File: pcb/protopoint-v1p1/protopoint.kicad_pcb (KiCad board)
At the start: 4 copper layers, 31.8 x 27.5 mm, 52 parts, among them T1 HHM1595A1, U1 STM32F031G4U6, U2 LXDC2HL, U3 DW1000, U4 SKY13317, U5 ProtoPoint_Module, X1 CRYSTAL_SMD_4, X2 CRYSTAL_SMD_4

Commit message: routing more signals out to castellations
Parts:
- C10, C17: value 12pF -> 100pF
- C11: value 12pF -> 10pF
- C16, C9: value 12pF -> 0.1uF
- C25, C26: value C_Small -> 12pF
- U1: value STM32F031G4U6 -> STM32F031G6U6
- X1: value CRYSTAL_SMD_4 -> 38.4M
- X2: value CRYSTAL_SMD_4 -> 16M
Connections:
- net V3P3 renamed VDD
- net VDDLDO1 renamed V1P8
- U5 pad 20: (no net) -> /SPI1_MOSI
- U5 pad 21: (no net) -> /SPI1_MISO
- U5 pad 22: (no net) -> /SPI1_CLK
- U5 pad 23: (no net) -> /~SPI1_SS
- U5 pad 24: (no net) -> /~DW_RST
- U5 pad 39: (no net) -> /DW_IRQ
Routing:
- net /SPI1_MOSI: track 11.0 -> 26.6 mm, vias 0 -> 1
- net /SPI1_MISO: track 11.4 -> 25.8 mm, vias 0 -> 1
- net /SPI1_CLK: track 11.8 -> 25.0 mm, vias 0 -> 1
- net /~SPI1_SS: track 8.28 -> 20.6 mm
- net /~DW_RST: track 5.01 -> 15.6 mm, vias 0 -> 1
- net V1P8: track 47.3 -> 41.5 mm
- net /DW_IRQ: track 13.1 -> 17.7 mm
- net VDD: track 137.5 -> 133.6 mm

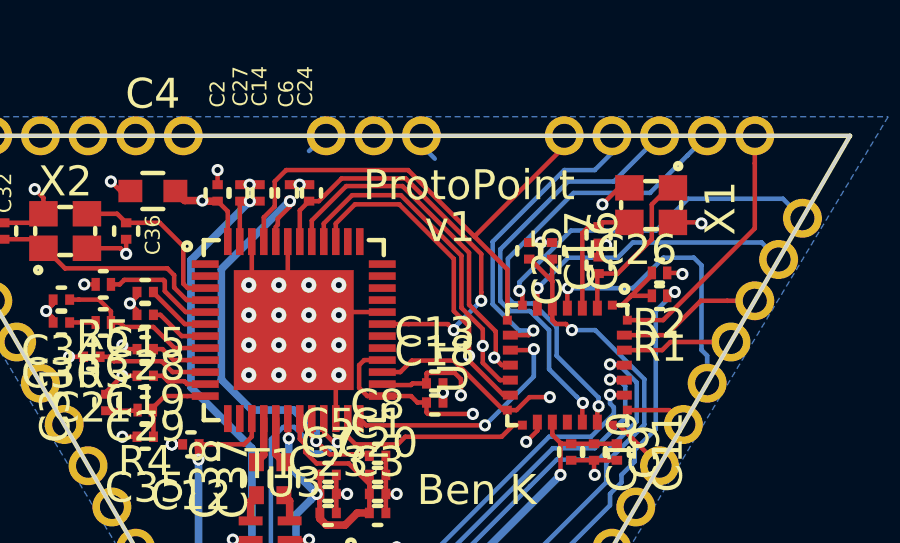
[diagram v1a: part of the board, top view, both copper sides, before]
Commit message: changing silkscreen version info
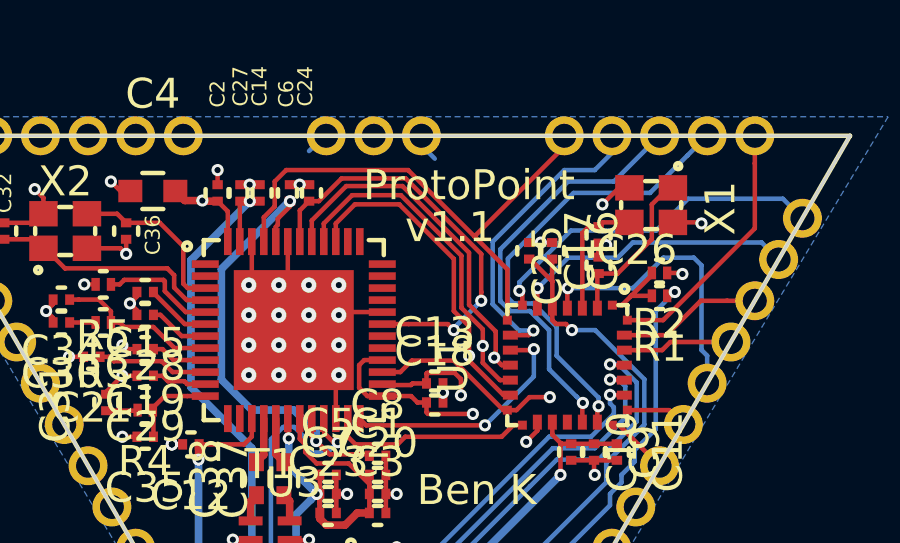
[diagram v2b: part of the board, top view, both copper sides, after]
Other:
- board text added: "v1.1"
- board text removed: "v1"
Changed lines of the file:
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@@
       (xy 1.582615 1.113693) (xy 1.582615 1.113693)) (layer F.SilkS) (width 0.1))
   )
-  (gr_text v1 (at 43.815 28.448) (layer F.SilkS)
+  (gr_text v1.1 (at 43.815 28.448) (layer F.SilkS)
     (effects (font (size 1 1) (thickness 0.2)))
   )

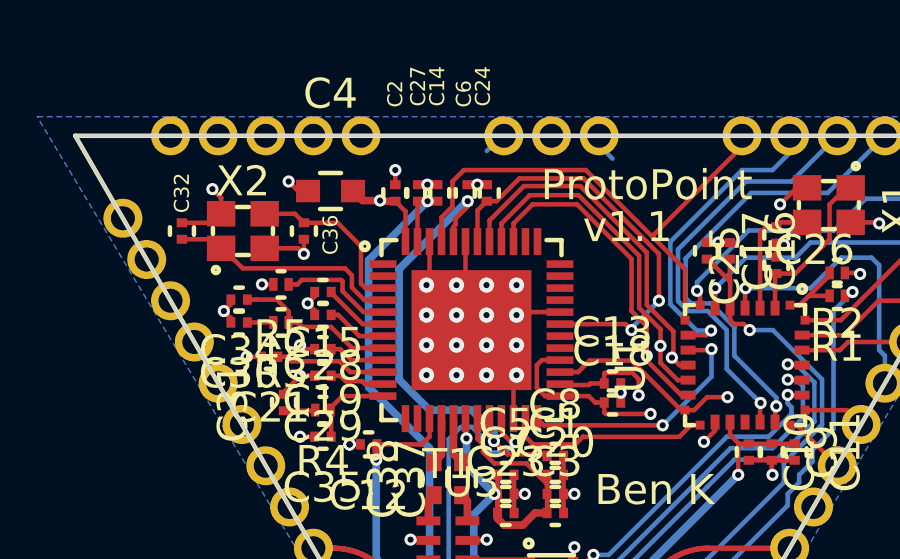
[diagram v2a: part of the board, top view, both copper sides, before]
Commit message: adding support for external clock and sync
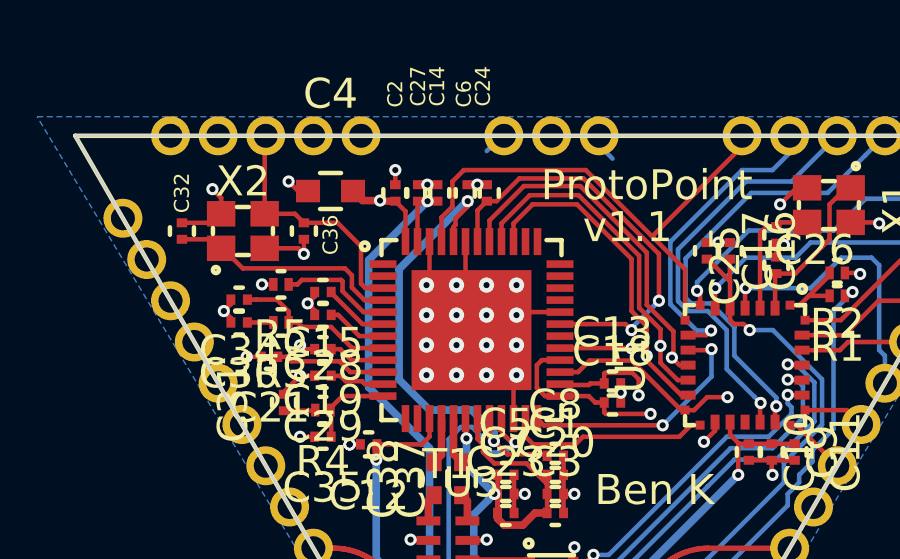
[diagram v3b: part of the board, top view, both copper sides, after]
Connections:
- net V1P8 renamed VDDLDO2
- net VDD renamed V3P3
- C36 pad 1: Net-(C36-Pad1) -> /DW_XTAL1
- U3 pad 29: (no net) -> /DW_SYNC
- U3 pad 3: Net-(C36-Pad1) -> /DW_XTAL1
- U5 pad 19: (no net) -> /DW_SYNC
- U5 pad 49: (no net) -> /DW_XTAL1
- X2 pad 3: Net-(C36-Pad1) -> /DW_XTAL1
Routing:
- net /DW_SYNC: track 0.00 -> 20.7 mm, vias 0 -> 1
- net /DW_XTAL1: track 0.00 -> 8.32 mm
- net Net-(C36-Pad1): track 5.70 -> 0.00 mm
